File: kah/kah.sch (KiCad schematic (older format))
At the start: 22 parts

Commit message: начата трассировка
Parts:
- added R1, R2, R3, R4: 20k_0805, N_RLC:Резистор_SMD_0805_0,125Вт, symbol elements:Резистор_0,125Вт
- added VT1, VT2: N-канал_IRLML6344TR, N_VD_HL:Транзистор_IRLML6344TR_SOT-23, symbol elements:Транзистор_полевой_N-IRLML6344TR
- added X1: Клеммник_х2, N_X:Клеммник_х2_шаг5, symbol elements:Клеммник_х2
- added XS1: Вилка_PLS8, N_X:Вилка_PLS8_вертикальная, symbol elements:Вилка_PLS8
- XS2: renamed from XS?; footprint (none) -> N_X:Розетка_RJ11_6P6C
- gave numbers to parts that had none: 21
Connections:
- net 5V: now also R1.1, R3.1
- net GND: now also R2.2, R4.2, VT1.2, VT2.2, XS1.6
- net 3V3: now reaches A1.14 (3.3)
- net 3V3: now also XS1.8
- net D13_SCK: now reaches A1.15 (D13/SCK)
- net D13_SCK: now also XS1.2
- net D2: now reaches A1.20 (D2)
- net D2: now also R3.2, VT2.3
- net D4: now reaches A1.22 (D4)
- net D4: now also R1.2, VT1.3
- net D7_IRQ: now reaches A1.25 (D7)
- net D7_IRQ: now also XS1.5
- net D8_RES: now reaches A1.26 (D8)
- net D8_RES: now also XS1.7
- net D10_SS: now reaches A1.28 (~D10/SS)
- net D10_SS: now also XS1.1
- net D11_MOSI: now reaches A1.29 (D11/MOSI)
- net D11_MOSI: now also XS1.3
- net D12_MISO: now reaches A1.30 (D12/MISO)
- net D12_MISO: now also XS1.4
- new net DI1: R2.1, VT1.1, X1.1
- new net DI2: R4.1, VT2.1, X1.2
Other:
- moved on the sheet: R7, R8, R9, VT3, XS2

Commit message: готова трассировка (50х55 мм)
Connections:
- net D2: now also R1.2, VT1.3; no longer R3.2, VT2.3
- net D3: now also R11.2, VT5.1; no longer R13.2, VT7.1
- net D4: now also R3.2, VT2.3; no longer R1.2, VT1.3
- net D5: now also R13.2, VT7.1; no longer R12.2, VT6.1
- net D6: now also R10.2, VT4.1; no longer R11.2, VT5.1
- net D9: now also R12.2, VT6.1; no longer R10.2, VT4.1
- net DOut_1: now also VT6.2, X5.1; no longer VT4.2, X4.1
- net DOut_2: now also VT7.2, X5.2; no longer VT5.2, X4.2
- net DOut_3: now also VT4.2, X4.1; no longer VT6.2, X5.1
- net DOut_4: now also VT5.2, X4.2; no longer VT7.2, X5.2
- net RS_Y: now also XS2.5; no longer XS2.6
- net RS_Z: now also XS2.6; no longer XS2.5
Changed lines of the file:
@@
 Wire Wire Line
 	14250 5000 14750 5000
+Text Label 14250 6500 0    50   ~ 0
+DOut_1
+Text Label 14250 6700 0    50   ~ 0
+DOut_2
+Wire Wire Line
+	14250 7350 14250 6700
+Wire Wire Line
+	14250 6700 14750 6700
 Text Label 14250 4800 0    50   ~ 0
-DOut_1
+DOut_3
 Text Label 14250 5000 0    50   ~ 0
-DOut_2
-Wire Wire Line
-	14250 7350 14250 6700
-Wire Wire Line
-	14250 6700 14750 6700
-Text Label 14250 6500 0    50   ~ 0
-DOut_3
-Text Label 14250 6700 0    50   ~ 0
 DOut_4
 $Comp
@@
 	12650 5100 11550 5100
 Connection ~ 12650 5100
+Text Label 11550 6800 2    50   ~ 0
+D9
+Wire Wire Line
+	12650 5950 11550 5950
 Text Label 11550 5100 2    50   ~ 0
-D9
-Wire Wire Line
-	12650 5950 11550 5950
-Text Label 11550 5950 2    50   ~ 0
 D6
 Connection ~ 12650 5950
 Wire Wire Line
 	12650 6800 11550 6800
-Text Label 11550 6800 2    50   ~ 0
+Text Label 11550 7650 2    50   ~ 0
 D5
 Connection ~ 12650 6800
 Wire Wire Line
 	12650 7650 11550 7650
-Text Label 11550 7650 2    50   ~ 0
+Text Label 11550 5950 2    50   ~ 0
 D3
 Connection ~ 12650 7650
@@
 Text Label 10200 3400 2    50   ~ 0
 RS_B
+Text Label 10200 3600 2    50   ~ 0
+RS_Z
 Text Label 10200 3500 2    50   ~ 0
-RS_Z
-Text Label 10200 3600 2    50   ~ 0
 RS_Y
 $Comp
@@
 Text Label 6200 6200 0    50   ~ 0
 D4
-Text Label 3500 5600 0    50   ~ 0
+Text Label 3500 7350 0    50   ~ 0
 D4
 Wire Wire Line
@@
 Text Label 6200 6500 0    50   ~ 0
 D2
-Text Label 3500 7350 0    50   ~ 0
+Text Label 3500 5600 0    50   ~ 0
 D2
 $EndSCHEMATC

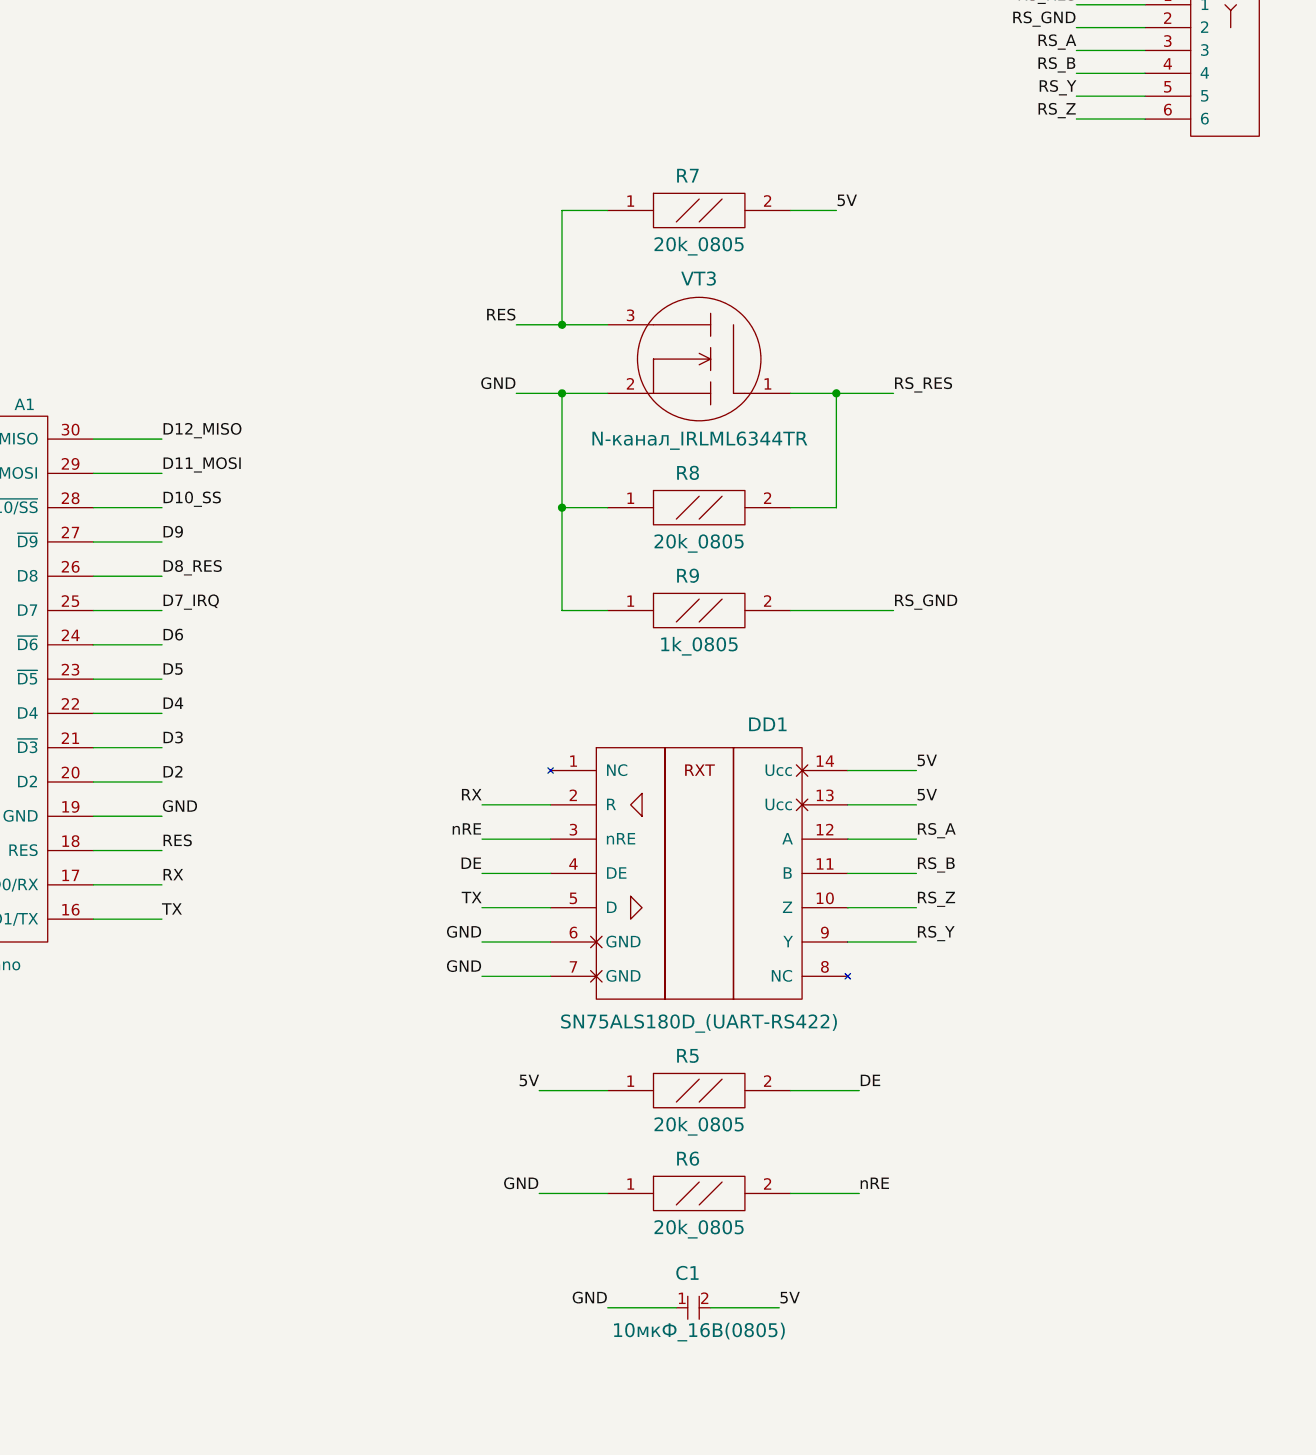
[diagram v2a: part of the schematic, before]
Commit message: добавлено согласующее сопротивление на RX - изменена версия
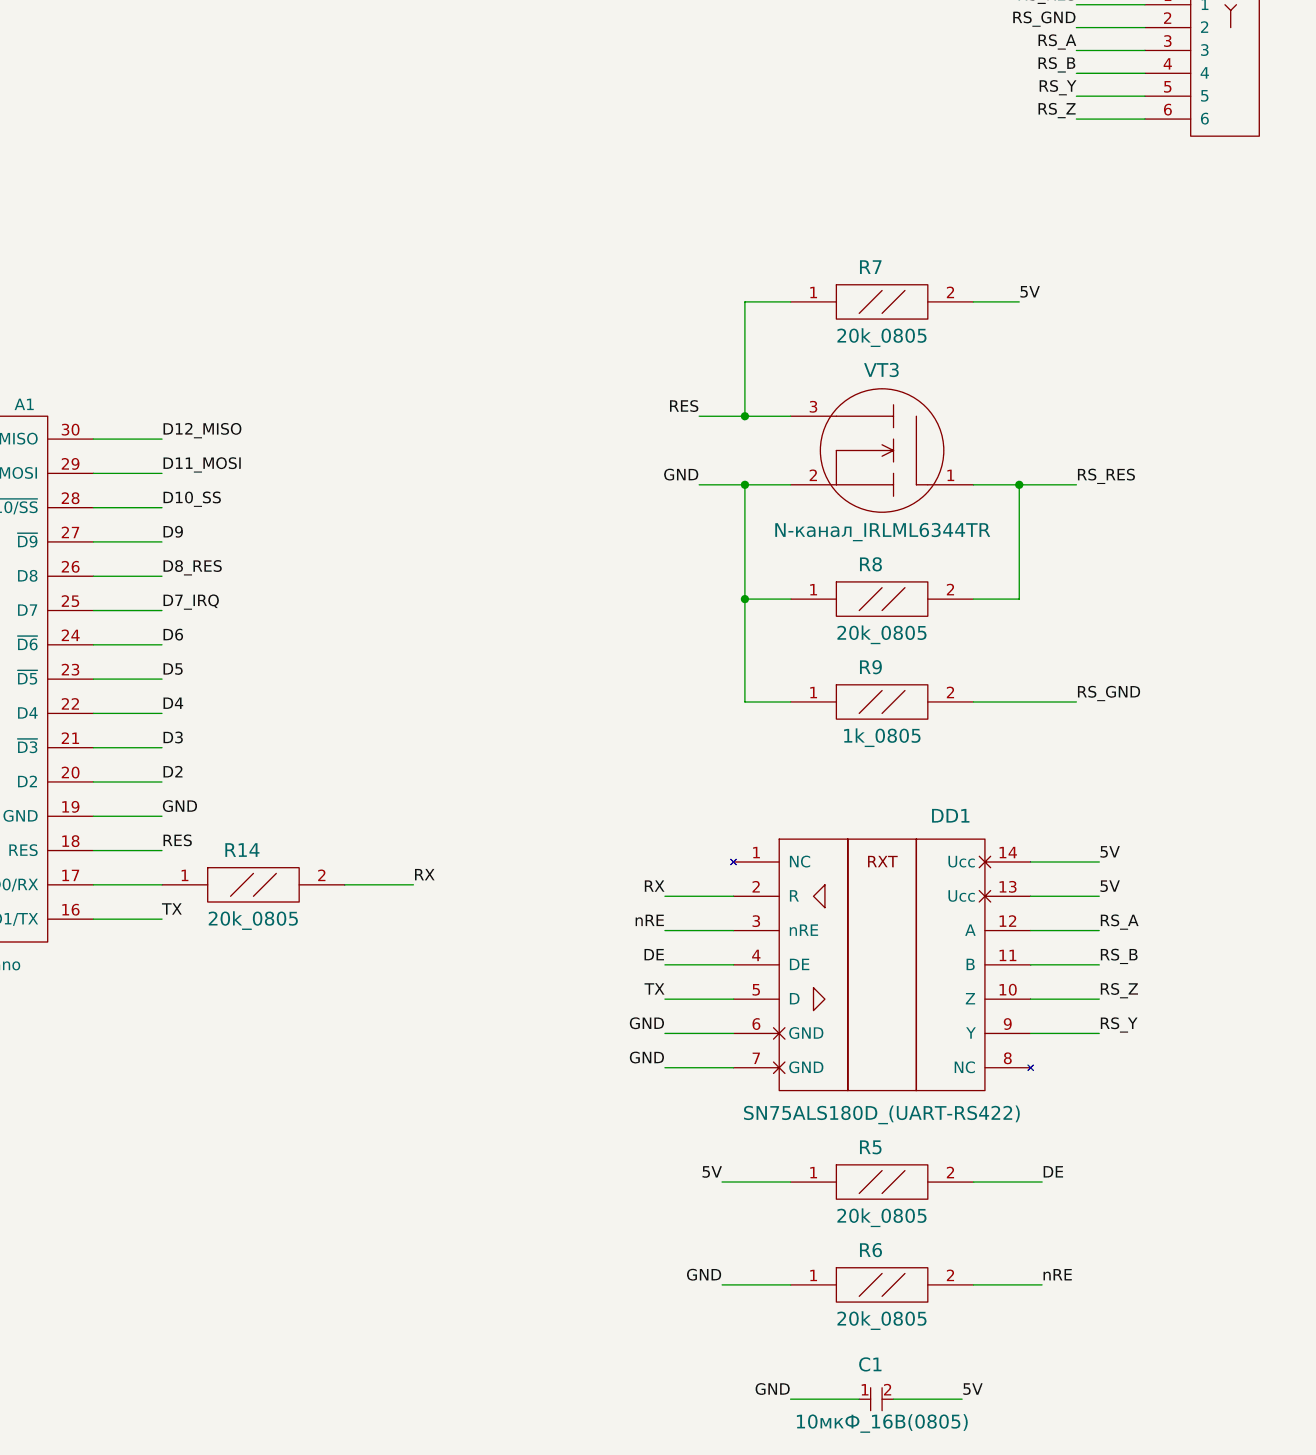
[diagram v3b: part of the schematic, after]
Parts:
- added R14: 20k_0805, N_RLC:Резистор_SMD_0805_0,125Вт, symbol elements:Резистор_0,125Вт
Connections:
- net RX: now also R14.2; no longer A1.17 (D0/RX)
- new net: A1.17 (D0/RX), R14.1
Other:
- moved on the sheet: C1, DD1, R5, R6, R7, R8, R9, VT3
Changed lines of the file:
@@
 L elements:Преобразователь_(UART-RS422) DD1
 U 1 1 5D3C9089
-P 8100 6450
-F 0 "DD1" H 8850 6650 60  0000 C CNN
-F 1 "SN75ALS180D_(UART-RS422)" H 8550 5350 60  0000 C CNN
-F 2 "N_DD:SO-14" H 8650 5950 60  0001 C CNN
-F 3 "" H 8650 5950 60  0001 C CNN
-	1    8100 6450
+P 8900 6850
+F 0 "DD1" H 9650 7050 60  0000 C CNN
+F 1 "SN75ALS180D_(UART-RS422)" H 9350 5750 60  0000 C CNN
+F 2 "N_DD:SO-14" H 9450 6350 60  0001 C CNN
+F 3 "" H 9450 6350 60  0001 C CNN
+	1    8900 6850
 	1    0    0    -1
 $EndComp
@@
 5V
 Wire Wire Line
-	9200 6450 9500 6450
-Wire Wire Line
-	9200 6600 9500 6600
-Wire Wire Line
-	7600 7200 7900 7200
-Wire Wire Line
-	7600 7350 7900 7350
-Text Label 7600 7200 2    50   ~ 0
-GND
-Text Label 7600 7350 2    50   ~ 0
-GND
-Text Label 9500 6450 0    50   ~ 0
-5V
-Text Label 9500 6600 0    50   ~ 0
+	10000 6850 10300 6850
+Wire Wire Line
+	10000 7000 10300 7000
+Wire Wire Line
+	8400 7600 8700 7600
+Wire Wire Line
+	8400 7750 8700 7750
+Text Label 8400 7600 2    50   ~ 0
+GND
+Text Label 8400 7750 2    50   ~ 0
+GND
+Text Label 10300 6850 0    50   ~ 0
+5V
+Text Label 10300 7000 0    50   ~ 0
 5V
 $Comp
 L elements:Резистор_0,125Вт R5
 U 1 1 5D3DE442
-P 8550 7850
-F 0 "R5" H 8500 8000 60  0000 C CNN
-F 1 "20k_0805" H 8550 7700 60  0000 C CNN
-F 2 "N_RLC:Резистор_SMD_0805_0,125Вт" H 8550 7850 60  0001 C CNN
-F 3 "" H 8550 7850 60  0001 C CNN
-	1    8550 7850
-	1    0    0    -1
-$EndComp
-Wire Wire Line
-	7600 6750 7900 6750
-Text Label 7600 6750 2    50   ~ 0
+P 9350 8250
+F 0 "R5" H 9300 8400 60  0000 C CNN
+F 1 "20k_0805" H 9350 8100 60  0000 C CNN
+F 2 "N_RLC:Резистор_SMD_0805_0,125Вт" H 9350 8250 60  0001 C CNN
+F 3 "" H 9350 8250 60  0001 C CNN
+	1    9350 8250
+	1    0    0    -1
+$EndComp
+Wire Wire Line
+	8400 7150 8700 7150
+Text Label 8400 7150 2    50   ~ 0
 nRE
 Wire Wire Line
-	7600 6900 7900 6900
-Text Label 7600 6900 2    50   ~ 0
+	8400 7300 8700 7300
+Text Label 8400 7300 2    50   ~ 0
 DE
 Wire Wire Line
-	8950 7850 9250 7850
-Text Label 9250 7850 0    50   ~ 0
+	9750 8250 10050 8250
+Text Label 10050 8250 0    50   ~ 0
 DE
 Wire Wire Line
-	7850 7850 8150 7850
-Text Label 7850 7850 2    50   ~ 0
+	8650 8250 8950 8250
+Text Label 8650 8250 2    50   ~ 0
 5V
 $Comp
 L elements:Резистор_0,125Вт R6
 U 1 1 5D3E5E9F
-P 8550 8300
-F 0 "R6" H 8500 8450 60  0000 C CNN
-F 1 "20k_0805" H 8550 8150 60  0000 C CNN
-F 2 "N_RLC:Резистор_SMD_0805_0,125Вт" H 8550 8300 60  0001 C CNN
-F 3 "" H 8550 8300 60  0001 C CNN
-	1    8550 8300
-	1    0    0    -1
-$EndComp
-Wire Wire Line
-	8950 8300 9250 8300
-Wire Wire Line
-	7850 8300 8150 8300
-Text Label 7850 8300 2    50   ~ 0
-GND
-Text Label 9250 8300 0    50   ~ 0
+P 9350 8700
+F 0 "R6" H 9300 8850 60  0000 C CNN
+F 1 "20k_0805" H 9350 8550 60  0000 C CNN
+F 2 "N_RLC:Резистор_SMD_0805_0,125Вт" H 9350 8700 60  0001 C CNN
+F 3 "" H 9350 8700 60  0001 C CNN
+	1    9350 8700
+	1    0    0    -1
+$EndComp
+Wire Wire Line
+	9750 8700 10050 8700
+Wire Wire Line
+	8650 8700 8950 8700
+Text Label 8650 8700 2    50   ~ 0
+GND
+Text Label 10050 8700 0    50   ~ 0
 nRE
 Wire Wire Line
-	7600 6600 7900 6600
-Text Label 7600 6600 2    50   ~ 0
+	8400 7000 8700 7000
+Text Label 8400 7000 2    50   ~ 0
 RX
 Wire Wire Line
-	7600 7050 7900 7050
-Text Label 7600 7050 2    50   ~ 0
+	8400 7450 8700 7450
+Text Label 8400 7450 2    50   ~ 0
 TX
-Text Label 6200 6950 0    50   ~ 0
-RX
 Text Label 6200 7100 0    50   ~ 0
 TX
@@
 L elements:Резистор_0,125Вт R8
 U 1 1 5D3F8F04
-P 8550 5300
-F 0 "R8" H 8500 5450 60  0000 C CNN
-F 1 "20k_0805" H 8550 5150 60  0000 C CNN
-F 2 "N_RLC:Резистор_SMD_0805_0,125Вт" H 8550 5300 60  0001 C CNN
-F 3 "" H 8550 5300 60  0001 C CNN
-	1    8550 5300
-	1    0    0    -1
-$EndComp
-Wire Wire Line
-	8950 4800 9150 4800
-Wire Wire Line
-	9150 4800 9150 5300
-Wire Wire Line
-	9150 5300 8950 5300
-Wire Wire Line
-	8150 5300 7950 5300
-Wire Wire Line
-	7950 5300 7950 4800
-Wire Wire Line
-	7950 4800 8150 4800
-Wire Wire Line
-	7950 4800 7750 4800
-Connection ~ 7950 4800
-Text Label 7750 4800 2    50   ~ 0
+P 9350 5700
+F 0 "R8" H 9300 5850 60  0000 C CNN
+F 1 "20k_0805" H 9350 5550 60  0000 C CNN
+F 2 "N_RLC:Резистор_SMD_0805_0,125Вт" H 9350 5700 60  0001 C CNN
+F 3 "" H 9350 5700 60  0001 C CNN
+	1    9350 5700
+	1    0    0    -1
+$EndComp
+Wire Wire Line
+	9750 5200 9950 5200
+Wire Wire Line
+	9950 5200 9950 5700
+Wire Wire Line
+	9950 5700 9750 5700
+Wire Wire Line
+	8950 5700 8750 5700
+Wire Wire Line
+	8750 5700 8750 5200
+Wire Wire Line
+	8750 5200 8950 5200
+Wire Wire Line
+	8750 5200 8550 5200
+Connection ~ 8750 5200
+Text Label 8550 5200 2    50   ~ 0
 GND
 $Comp
 L elements:Резистор_0,125Вт R9
 U 1 1 5D4006CB
-P 8550 5750
-F 0 "R9" H 8500 5900 60  0000 C CNN
-F 1 "1k_0805" H 8550 5600 60  0000 C CNN
-F 2 "N_RLC:Резистор_SMD_0805_0,125Вт" H 8550 5750 60  0001 C CNN
-F 3 "" H 8550 5750 60  0001 C CNN
-	1    8550 5750
-	1    0    0    -1
-$EndComp
-Wire Wire Line
-	7950 5300 7950 5750
-Wire Wire Line
-	7950 5750 8150 5750
-Connection ~ 7950 5300
-Wire Wire Line
-	9200 6750 9500 6750
-Wire Wire Line
-	9200 6900 9500 6900
-Wire Wire Line
-	9200 7050 9500 7050
-Wire Wire Line
-	9200 7200 9500 7200
-Text Label 9500 6750 0    50   ~ 0
+P 9350 6150
+F 0 "R9" H 9300 6300 60  0000 C CNN
+F 1 "1k_0805" H 9350 6000 60  0000 C CNN
+F 2 "N_RLC:Резистор_SMD_0805_0,125Вт" H 9350 6150 60  0001 C CNN
+F 3 "" H 9350 6150 60  0001 C CNN
+	1    9350 6150
+	1    0    0    -1
+$EndComp
+Wire Wire Line
+	8750 5700 8750 6150
+Wire Wire Line
+	8750 6150 8950 6150
+Connection ~ 8750 5700
+Wire Wire Line
+	10000 7150 10300 7150
+Wire Wire Line
+	10000 7300 10300 7300
+Wire Wire Line
+	10000 7450 10300 7450
+Wire Wire Line
+	10000 7600 10300 7600
+Text Label 10300 7150 0    50   ~ 0
 RS_A
-Text Label 9500 6900 0    50   ~ 0
+Text Label 10300 7300 0    50   ~ 0
 RS_B
-Text Label 9500 7050 0    50   ~ 0
+Text Label 10300 7450 0    50   ~ 0
 RS_Z
-Text Label 9500 7200 0    50   ~ 0
+Text Label 10300 7600 0    50   ~ 0
 RS_Y
 Wire Wire Line
@@
 Text Label 6200 6800 0    50   ~ 0
 RES
-Text Label 7750 4500 2    50   ~ 0
+Text Label 8550 4900 2    50   ~ 0
 RES
 Wire Wire Line
-	8150 4500 7950 4500
+	8950 4900 8750 4900
 $Comp
 L elements:Резистор_0,125Вт R7
 U 1 1 5D40F658
-P 8550 4000
-F 0 "R7" H 8500 4150 60  0000 C CNN
-F 1 "20k_0805" H 8550 3850 60  0000 C CNN
-F 2 "N_RLC:Резистор_SMD_0805_0,125Вт" H 8550 4000 60  0001 C CNN
-F 3 "" H 8550 4000 60  0001 C CNN
-	1    8550 4000
-	1    0    0    -1
-$EndComp
-Wire Wire Line
-	8150 4000 7950 4000
-Wire Wire Line
-	7950 4000 7950 4500
-Connection ~ 7950 4500
-Wire Wire Line
-	7950 4500 7750 4500
-Wire Wire Line
-	8950 4000 9150 4000
-Text Label 9150 4000 0    50   ~ 0
-5V
-Wire Wire Line
-	8950 5750 9400 5750
-Text Label 9400 5750 0    50   ~ 0
+P 9350 4400
+F 0 "R7" H 9300 4550 60  0000 C CNN
+F 1 "20k_0805" H 9350 4250 60  0000 C CNN
+F 2 "N_RLC:Резистор_SMD_0805_0,125Вт" H 9350 4400 60  0001 C CNN
+F 3 "" H 9350 4400 60  0001 C CNN
+	1    9350 4400
+	1    0    0    -1
+$EndComp
+Wire Wire Line
+	8950 4400 8750 4400
+Wire Wire Line
+	8750 4400 8750 4900
+Connection ~ 8750 4900
+Wire Wire Line
+	8750 4900 8550 4900
+Wire Wire Line
+	9750 4400 9950 4400
+Text Label 9950 4400 0    50   ~ 0
+5V
+Wire Wire Line
+	9750 6150 10200 6150
+Text Label 10200 6150 0    50   ~ 0
 RS_GND
 Wire Wire Line
-	9150 4800 9400 4800
-Connection ~ 9150 4800
-Text Label 9400 4800 0    50   ~ 0
+	9950 5200 10200 5200
+Connection ~ 9950 5200
+Text Label 10200 5200 0    50   ~ 0
 RS_RES
 $Comp
 L elements:Транзистор_полевой_N-IRLML6344TR VT3
 U 1 1 5D41C7EA
-P 8700 4800
-F 0 "VT3" H 8850 5300 60  0000 C CNN
-F 1 "N-канал_IRLML6344TR" H 8850 4600 60  0000 C CNN
-F 2 "N_VD_HL:Транзистор_IRLML6344TR_SOT-23" H 8700 4800 60  0001 C CNN
-F 3 "" H 8700 4800 60  0001 C CNN
-	1    8700 4800
+P 9500 5200
+F 0 "VT3" H 9650 5700 60  0000 C CNN
+F 1 "N-канал_IRLML6344TR" H 9650 5000 60  0000 C CNN
+F 2 "N_VD_HL:Транзистор_IRLML6344TR_SOT-23" H 9500 5200 60  0001 C CNN
+F 3 "" H 9500 5200 60  0001 C CNN
+	1    9500 5200
 	-1   0    0    -1
 $EndComp
@@
 L elements:Конденсатор_керамический C1
 U 1 1 5D445384
-P 8500 8800
-F 0 "C1" H 8500 8950 60  0000 C CNN
-F 1 "10мкФ_16В(0805)" H 8550 8700 60  0000 C CNN
-F 2 "N_RLC:Конденсатор_SMD_0805" H 8500 8800 60  0001 C CNN
-F 3 "" H 8500 8800 60  0001 C CNN
-	1    8500 8800
-	1    0    0    -1
-$EndComp
-Wire Wire Line
-	8150 8800 8450 8800
-Wire Wire Line
-	8600 8800 8900 8800
-Text Label 8150 8800 2    50   ~ 0
-GND
-Text Label 8900 8800 0    50   ~ 0
+P 9300 9200
+F 0 "C1" H 9300 9350 60  0000 C CNN
+F 1 "10мкФ_16В(0805)" H 9350 9100 60  0000 C CNN
+F 2 "N_RLC:Конденсатор_SMD_0805" H 9300 9200 60  0001 C CNN
+F 3 "" H 9300 9200 60  0001 C CNN
+	1    9300 9200
+	1    0    0    -1
+$EndComp
+Wire Wire Line
+	8950 9200 9250 9200
+Wire Wire Line
+	9400 9200 9700 9200
+Text Label 8950 9200 2    50   ~ 0
+GND
+Text Label 9700 9200 0    50   ~ 0
 5V
 $Comp
@@
 Text Label 3500 5600 0    50   ~ 0
 D2
+$Comp
+L elements:Резистор_0,125Вт R14
+U 1 1 5D4A5A0D
+P 6600 6950
+F 0 "R14" H 6550 7100 60  0000 C CNN
+F 1 "20k_0805" H 6600 6800 60  0000 C CNN
+F 2 "N_RLC:Резистор_SMD_0805_0,125Вт" H 6600 6950 60  0001 C CNN
+F 3 "" H 6600 6950 60  0001 C CNN
+	1    6600 6950
+	1    0    0    -1
+$EndComp
+Text Label 7300 6950 0    50   ~ 0
+RX
+Wire Wire Line
+	7000 6950 7300 6950
 $EndSCHEMATC
